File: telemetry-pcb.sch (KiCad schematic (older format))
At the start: 23 parts, among them J1 1x04

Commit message: replaced headers with screw terminals, placed 12v off board
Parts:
- removed ECU_UART, THERMO_IN_1, THERMO_IN_2: PINHD-1X2, telemetry-pcb:1X02, symbol telemetry-pcb-eagle-import:PINHD-1X2
- removed J1, J? (x5): 1x04, symbol Connector_Generic:Conn_01x04
- added 12V_IN, CAN_INOUT1, CAN_INOUT2, CAN_INOUT3, CAN_INOUT4, CAN_INOUT5, CAN_INOUT6, ECU_RS232, THERMO_IN1, THERMO_IN2: 1x02, symbol Connector:Screw_Terminal_01x02
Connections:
- net labels removed: +12V
- wire segments 140 -> 119

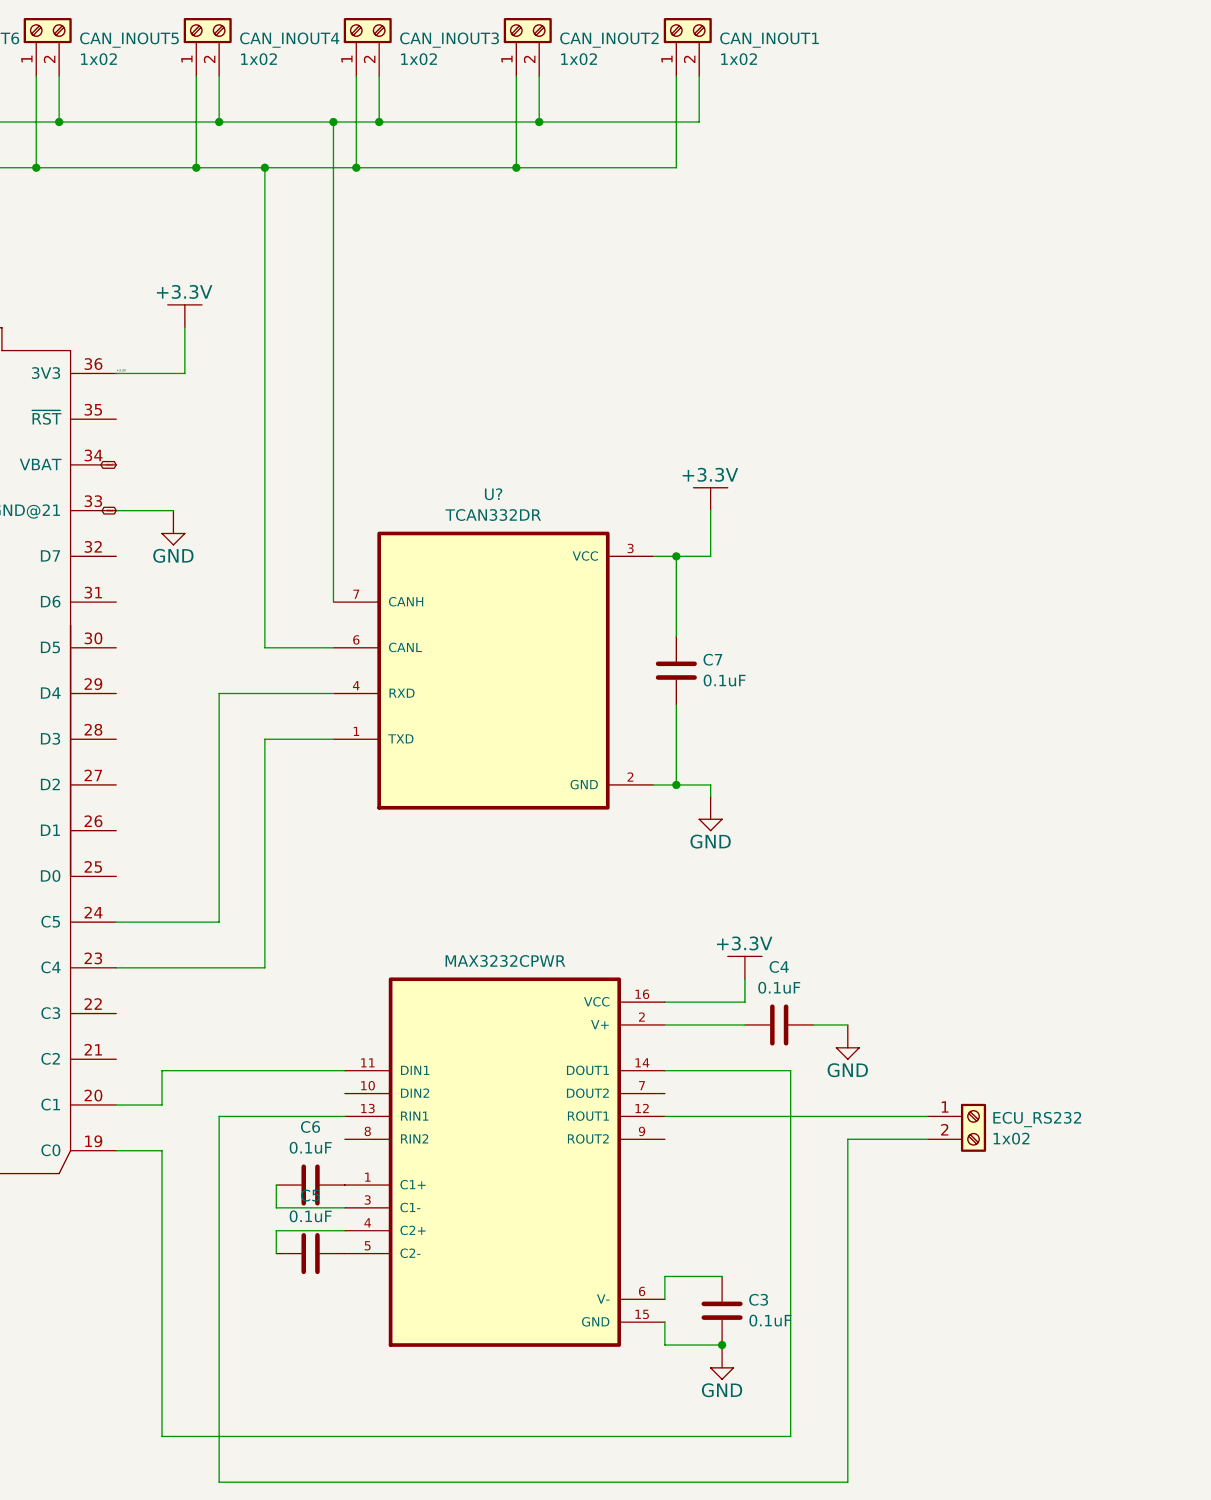
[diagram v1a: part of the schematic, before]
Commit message: finished schematic with 12v off-board input and outputs as specified on Notion
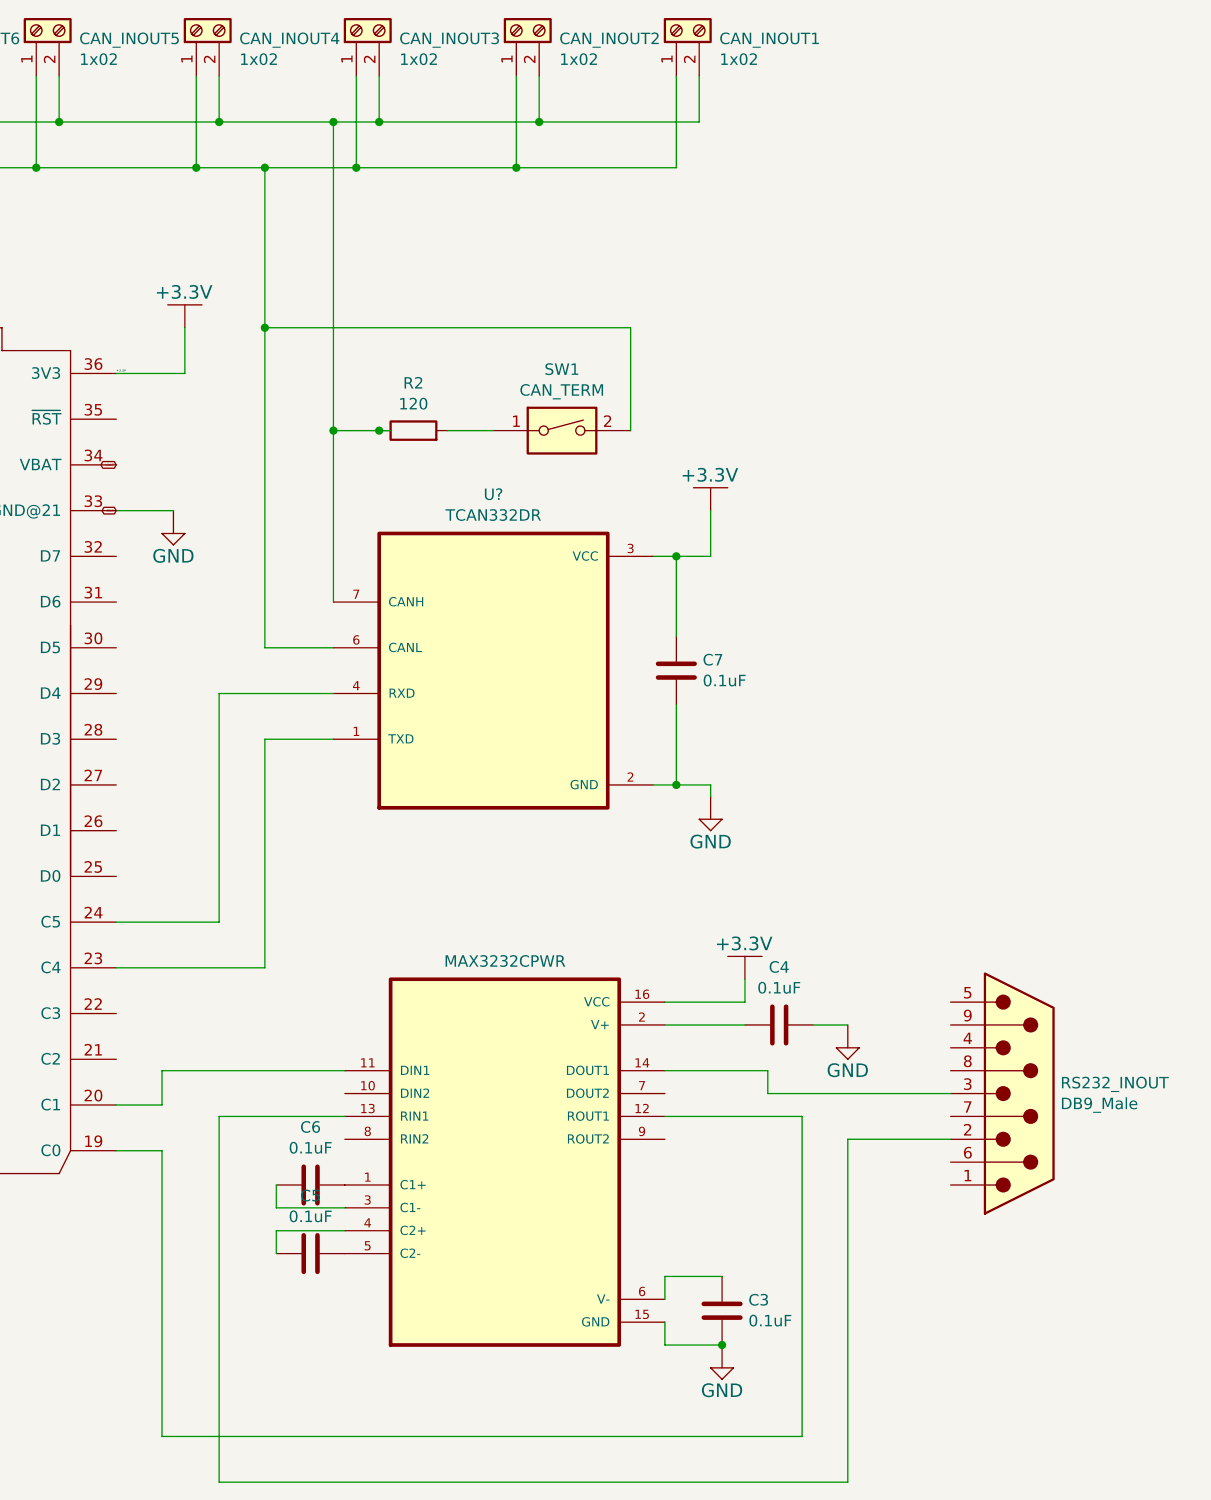
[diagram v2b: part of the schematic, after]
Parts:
- removed ECU_RS232: 1x02, symbol Connector:Screw_Terminal_01x02
- added R2: 120, symbol Device:R
- added RS232_INOUT: DB9_Male, symbol Connector:DB9_Male
- added SW1: CAN_TERM, symbol Switch:SW_DIP_x01
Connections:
- net at U$1.19 (C0): now also U?.12 (ROUT1); no longer U?.14 (DOUT1)
- net at U?.13 (RIN1): now also RS232_INOUT.2
- net at CAN_INOUT1.1 (Pin_1), CAN_INOUT2.1 (Pin_1), CAN_INOUT3.1 (Pin_1)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: now also SW1.2
- net at CAN_INOUT1.2 (Pin_2), CAN_INOUT2.2 (Pin_2), CAN_INOUT3.2 (Pin_2)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: now also R2.1
- new net: RS232_INOUT.3, U?.14 (DOUT1)
- new net: R2.2, SW1.1
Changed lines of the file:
@@
 	7100 3100 7350 3100
-$Comp
-L MAX3232CPWR:MAX3232CPWR U?
-U 1 1 600C0311
-P 8800 5950
-F 0 "U?" H 8800 6920 50  0001 C CNN
-F 1 "MAX3232CPWR" H 8800 6828 50  0000 C CNN
-F 2 "SOP65P640X120-16N" H 8800 5950 50  0001 L BNN
-F 3 "" H 8800 5950 50  0001 L BNN
-	1    8800 5950
-	1    0    0    -1
-$EndComp
 $Comp
 L telemetry-pcb-eagle-import:+3.3V #SUPPLY?
@@
 Wire Wire Line
 	7300 5900 7300 7150
-Wire Wire Line
-	7300 7150 10050 7150
-Wire Wire Line
-	10050 7150 10050 5550
-Wire Wire Line
-	10050 5550 9500 5550
-Wire Wire Line
-	9500 5750 10650 5750
-Wire Wire Line
-	8100 5750 7550 5750
-Wire Wire Line
-	7550 5750 7550 7350
 Wire Wire Line
 	7550 7350 10300 7350
@@
 Wire Wire Line
 	7800 6250 8100 6250
-Wire Wire Line
-	10650 5850 10300 5850
-Wire Wire Line
-	10300 5850 10300 7350
 $Comp
 L telemetry-pcb-eagle-import:+3.3V #SUPPLY?
@@
 Wire Wire Line
 	7550 3900 8050 3900
-Wire Wire Line
-	8050 3500 8050 1400
 Connection ~ 8050 1400
 Wire Wire Line
 	8050 3700 7750 3700
 Wire Wire Line
-	7750 3700 7750 1600
+	7750 3700 7750 2300
 Connection ~ 7750 1600
 $Comp
@@
 	2500 5700 3300 5700
 $Comp
-L Connector:Screw_Terminal_01x02 ECU_RS232
-U 1 1 6010097F
-P 10850 5750
-F 0 "ECU_RS232" H 10930 5742 50  0000 L CNN
-F 1 "1x02" H 10930 5651 50  0000 L CNN
-F 2 "" H 10850 5750 50  0001 C CNN
-F 3 "~" H 10850 5750 50  0001 C CNN
-	1    10850 5750
-	1    0    0    -1
-$EndComp
-$Comp
 L Connector:Screw_Terminal_01x02 12V_IN
 U 1 1 60109049
@@
 Wire Wire Line
 	9550 1600 9550 1200
+$Comp
+L Connector:DB9_Male RS232_INOUT
+U 1 1 600D7019
+P 11050 5650
+F 0 "RS232_INOUT" H 11230 5696 50  0000 L CNN
+F 1 "DB9_Male" H 11230 5605 50  0000 L CNN
+F 2 "" H 11050 5650 50  0001 C CNN
+F 3 " ~" H 11050 5650 50  0001 C CNN
+	1    11050 5650
+	1    0    0    -1
+$EndComp
+Wire Wire Line
+	10100 7150 10100 5750
+Wire Wire Line
+	10100 5750 9500 5750
+Wire Wire Line
+	7300 7150 10100 7150
+$Comp
+L MAX3232CPWR:MAX3232CPWR U?
+U 1 1 600C0311
+P 8800 5950
+F 0 "U?" H 8800 6920 50  0001 C CNN
+F 1 "MAX3232CPWR" H 8800 6828 50  0000 C CNN
+F 2 "SOP65P640X120-16N" H 8800 5950 50  0001 L BNN
+F 3 "" H 8800 5950 50  0001 L BNN
+	1    8800 5950
+	1    0    0    -1
+$EndComp
+Wire Wire Line
+	9500 5550 9950 5550
+Wire Wire Line
+	9950 5550 9950 5650
+Wire Wire Line
+	9950 5650 10750 5650
+Wire Wire Line
+	8100 5750 7550 5750
+Wire Wire Line
+	7550 5750 7550 7350
+Wire Wire Line
+	10300 7350 10300 5850
+Wire Wire Line
+	10300 5850 10750 5850
+$Comp
+L Switch:SW_DIP_x01 SW1
+U 1 1 600F3419
+P 9050 2750
+F 0 "SW1" H 9050 3017 50  0000 C CNN
+F 1 "CAN_TERM" H 9050 2926 50  0000 C CNN
+F 2 "" H 9050 2750 50  0001 C CNN
+F 3 "~" H 9050 2750 50  0001 C CNN
+	1    9050 2750
+	1    0    0    -1
+$EndComp
+Connection ~ 7750 2300
+Wire Wire Line
+	7750 2300 7750 1600
+Wire Wire Line
+	8050 1400 8050 2750
+$Comp
+L Device:R R2
+U 1 1 600CBD97
+P 8400 2750
+F 0 "R2" V 8607 2750 50  0000 C CNN
+F 1 "120" V 8516 2750 50  0000 C CNN
+F 2 "" V 8330 2750 50  0001 C CNN
+F 3 "~" H 8400 2750 50  0001 C CNN
+	1    8400 2750
+	0    -1   -1   0
+$EndComp
+Wire Wire Line
+	8050 2750 8250 2750
+Connection ~ 8050 2750
+Wire Wire Line
+	8050 2750 8050 3500
+Wire Wire Line
+	9350 2750 9350 2300
+Wire Wire Line
+	7750 2300 9350 2300
+Connection ~ 8250 2750
+Wire Wire Line
+	8250 2750 8300 2750
+Wire Wire Line
+	8550 2750 8750 2750
 $EndSCHEMATC

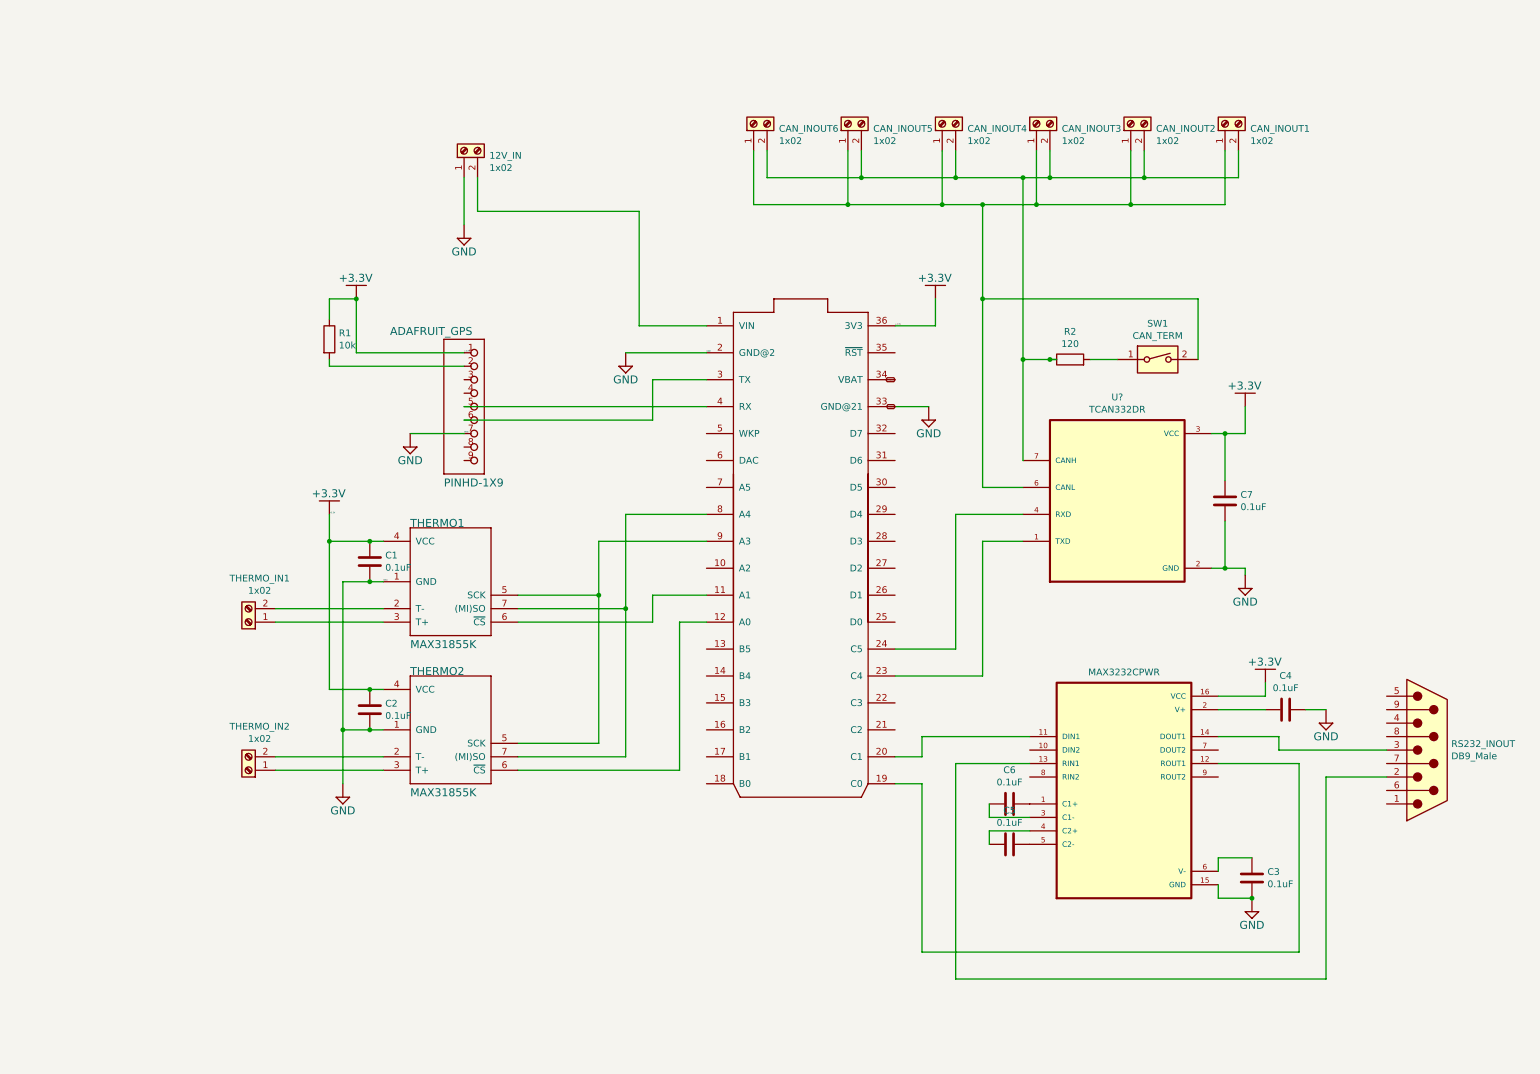
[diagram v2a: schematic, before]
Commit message: finished schematic with 12v off-board input and outputs as specified on Notion
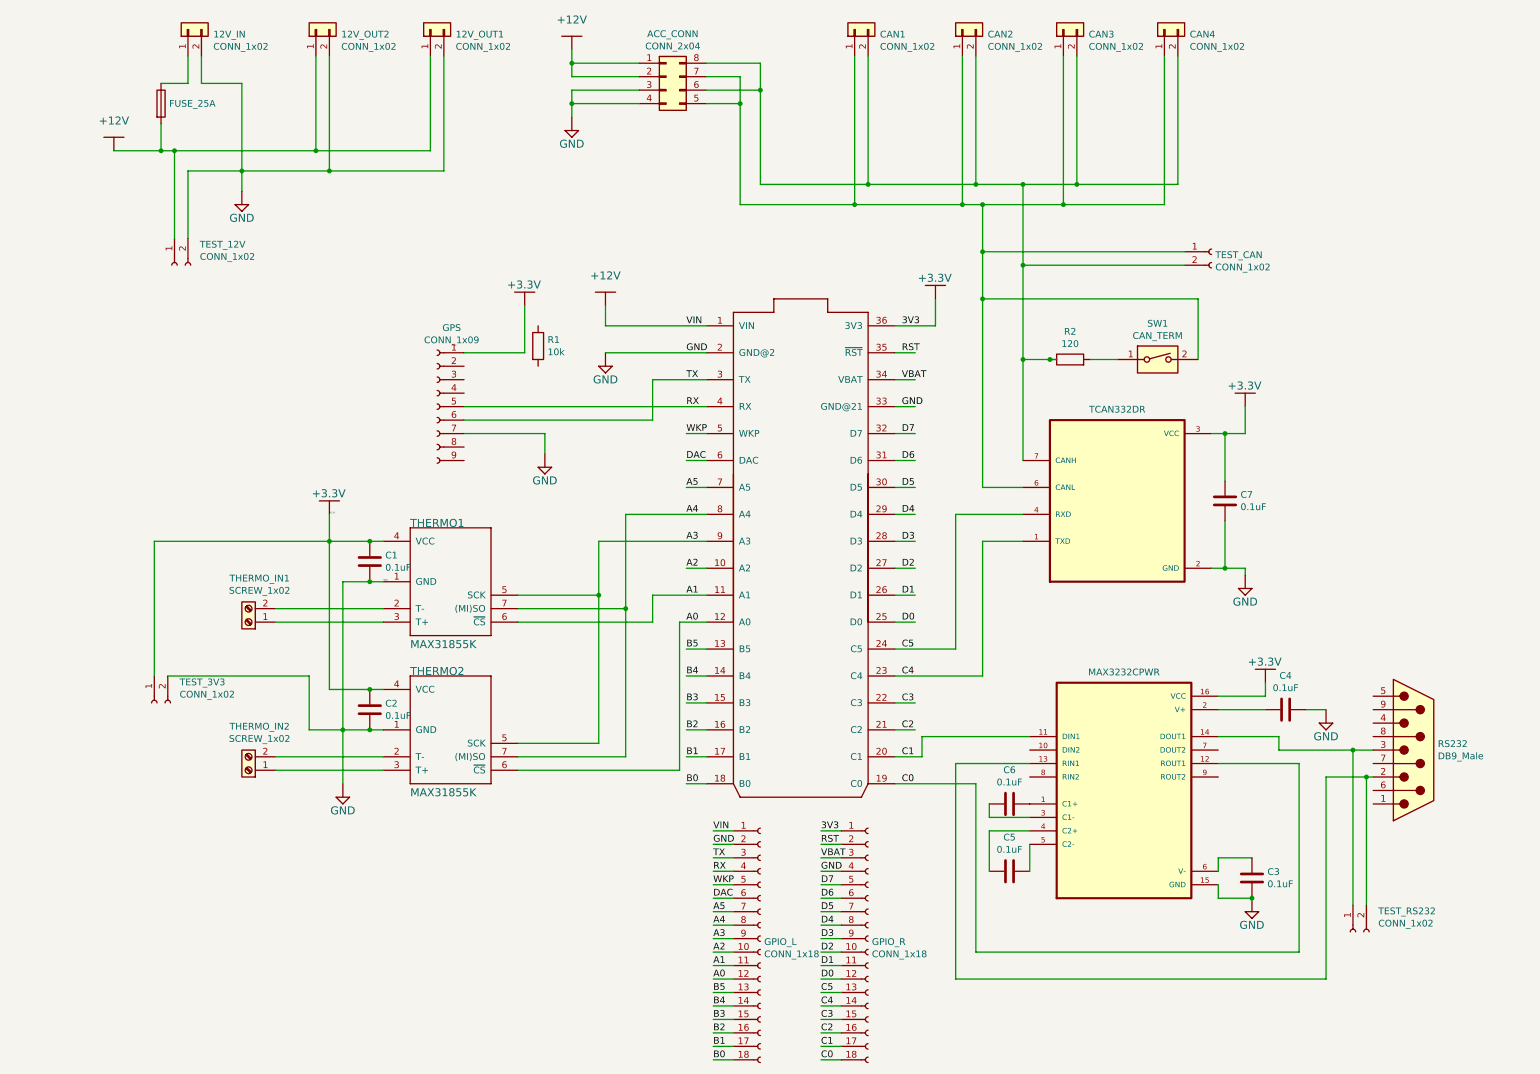
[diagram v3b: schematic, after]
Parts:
- removed 12V_IN, CAN_INOUT1, CAN_INOUT2, CAN_INOUT3, CAN_INOUT4, CAN_INOUT5, CAN_INOUT6: 1x02, symbol Connector:Screw_Terminal_01x02
- removed ADAFRUIT_GPS: PINHD-1X9, telemetry-pcb:1X09-BIG, symbol telemetry-pcb-eagle-import:PINHD-1X9
- added 12V_IN, 12V_OUT1, 12V_OUT2, CAN1, CAN2, CAN3, CAN4: CONN_1x02, symbol Connector_Generic:Conn_01x02
- added ACC_CONN: CONN_2x04, symbol Connector_Generic:Conn_02x04_Counter_Clockwise
- added F?: FUSE_25A, symbol Device:Fuse
- added GPIO_L, GPIO_R: CONN_1x18, symbol Connector:Conn_01x18_Female
- added GPS: CONN_1x09, symbol Connector:Conn_01x09_Female
- added TEST_12V, TEST_3V3, TEST_CAN, TEST_RS232: CONN_1x02, symbol Connector:Conn_01x02_Female
- THERMO_IN1, THERMO_IN2: value 1x02 -> SCREW_1x02
- renumbered RS232_INOUT to RS232
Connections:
- net labels added: +12V, 3V3, A0, A1, A2, A3, A4, A5, B0, B1, B2, B3, B4, B5, C0, C1, C2, C3, C4, C5, D0, D1, D2, D3, D4, D5, D6, D7, DAC, RST, RX, TX, VIN, WKP
- wire segments 128 -> 224
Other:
- moved on the sheet: C5, R1, RS232

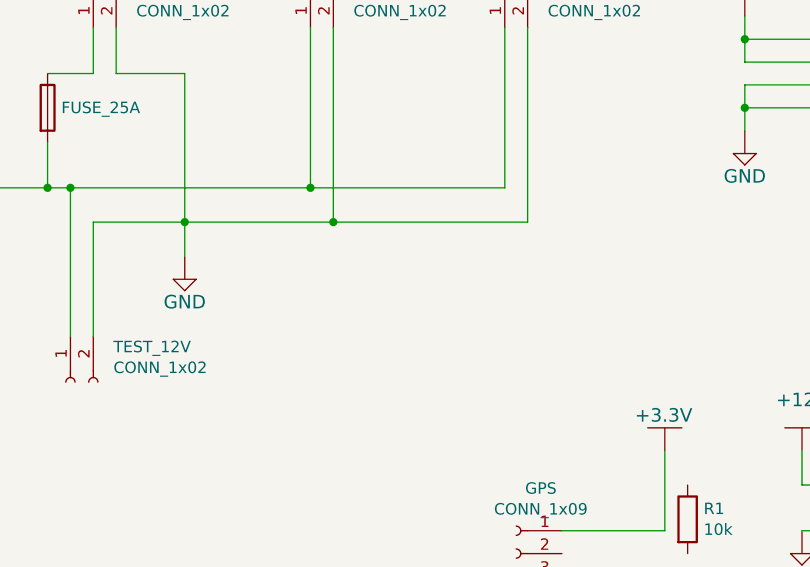
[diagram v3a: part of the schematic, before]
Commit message: added fan connector
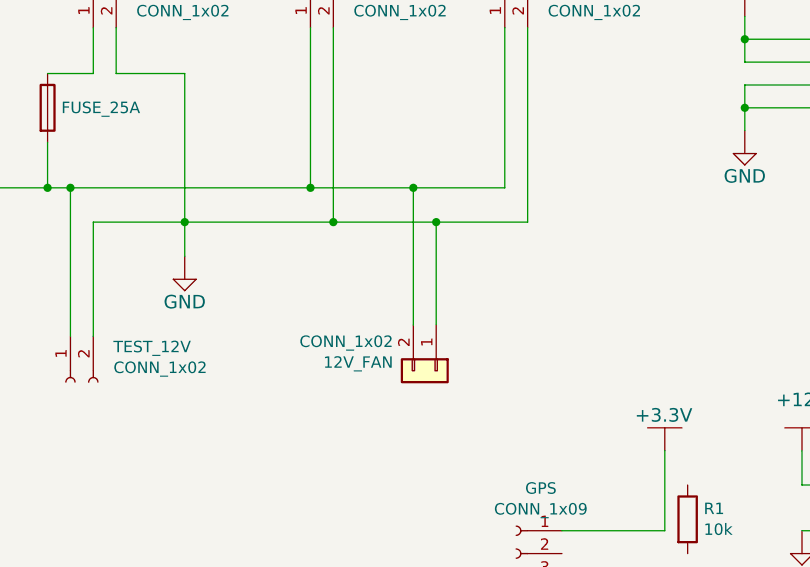
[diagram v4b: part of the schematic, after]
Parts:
- added 12V_FAN: CONN_1x02, symbol Connector_Generic:Conn_01x02
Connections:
- wire segments 224 -> 228
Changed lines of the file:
@@
 	2800 500  2800 1200
 Wire Wire Line
-	2800 1200 3650 1200
+	2800 1200 3250 1200
 Wire Wire Line
 	3650 500  3650 1200
@@
 	2250 1350 2250 1500
 Wire Wire Line
-	2900 1350 3750 1350
+	2900 1350 3350 1350
 Wire Wire Line
 	3750 1350 3750 500
@@
 Wire Wire Line
 	2750 5500 3000 5500
+$Comp
+L Connector_Generic:Conn_01x02 12V_FAN
+U 1 1 60791D32
+P 3350 2000
+F 0 "12V_FAN" V 3314 1812 50  0000 R CNN
+F 1 "CONN_1x02" V 3223 1812 50  0000 R CNN
+F 2 "" H 3350 2000 50  0001 C CNN
+F 3 "~" H 3350 2000 50  0001 C CNN
+	1    3350 2000
+	0    1    1    0
+$EndComp
+Wire Wire Line
+	3350 1800 3350 1350
+Connection ~ 3350 1350
+Wire Wire Line
+	3350 1350 3750 1350
+Wire Wire Line
+	3250 1800 3250 1200
+Connection ~ 3250 1200
+Wire Wire Line
+	3250 1200 3650 1200
 $EndSCHEMATC
